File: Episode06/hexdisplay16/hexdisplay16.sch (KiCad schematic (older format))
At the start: 28 parts, among them J1 Conn_01x05, J10 Conn_01x16, J2 Conn_01x05, J3 Conn_01x05, J4 Conn_01x05, J5 Conn_01x05, J6 Conn_01x05, J7 Conn_01x05, J8 Conn_01x05, J9 Conn_01x02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

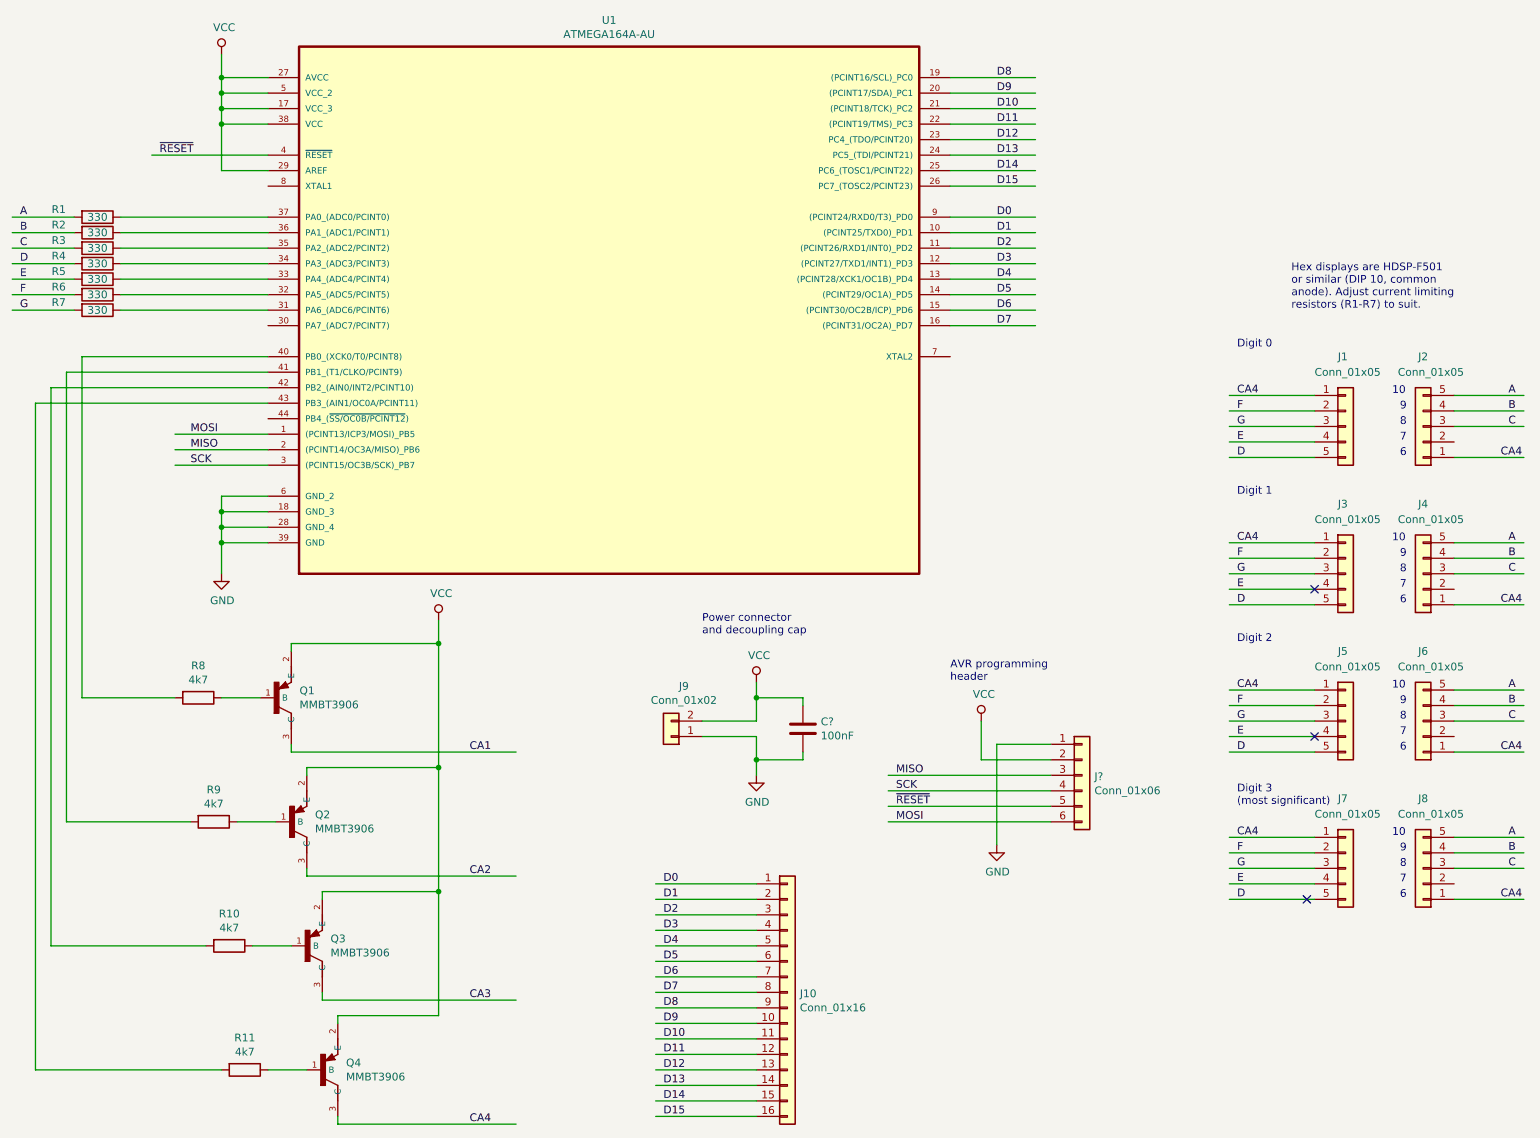
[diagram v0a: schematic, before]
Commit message: use proper DIP-10 connectors for hex displays
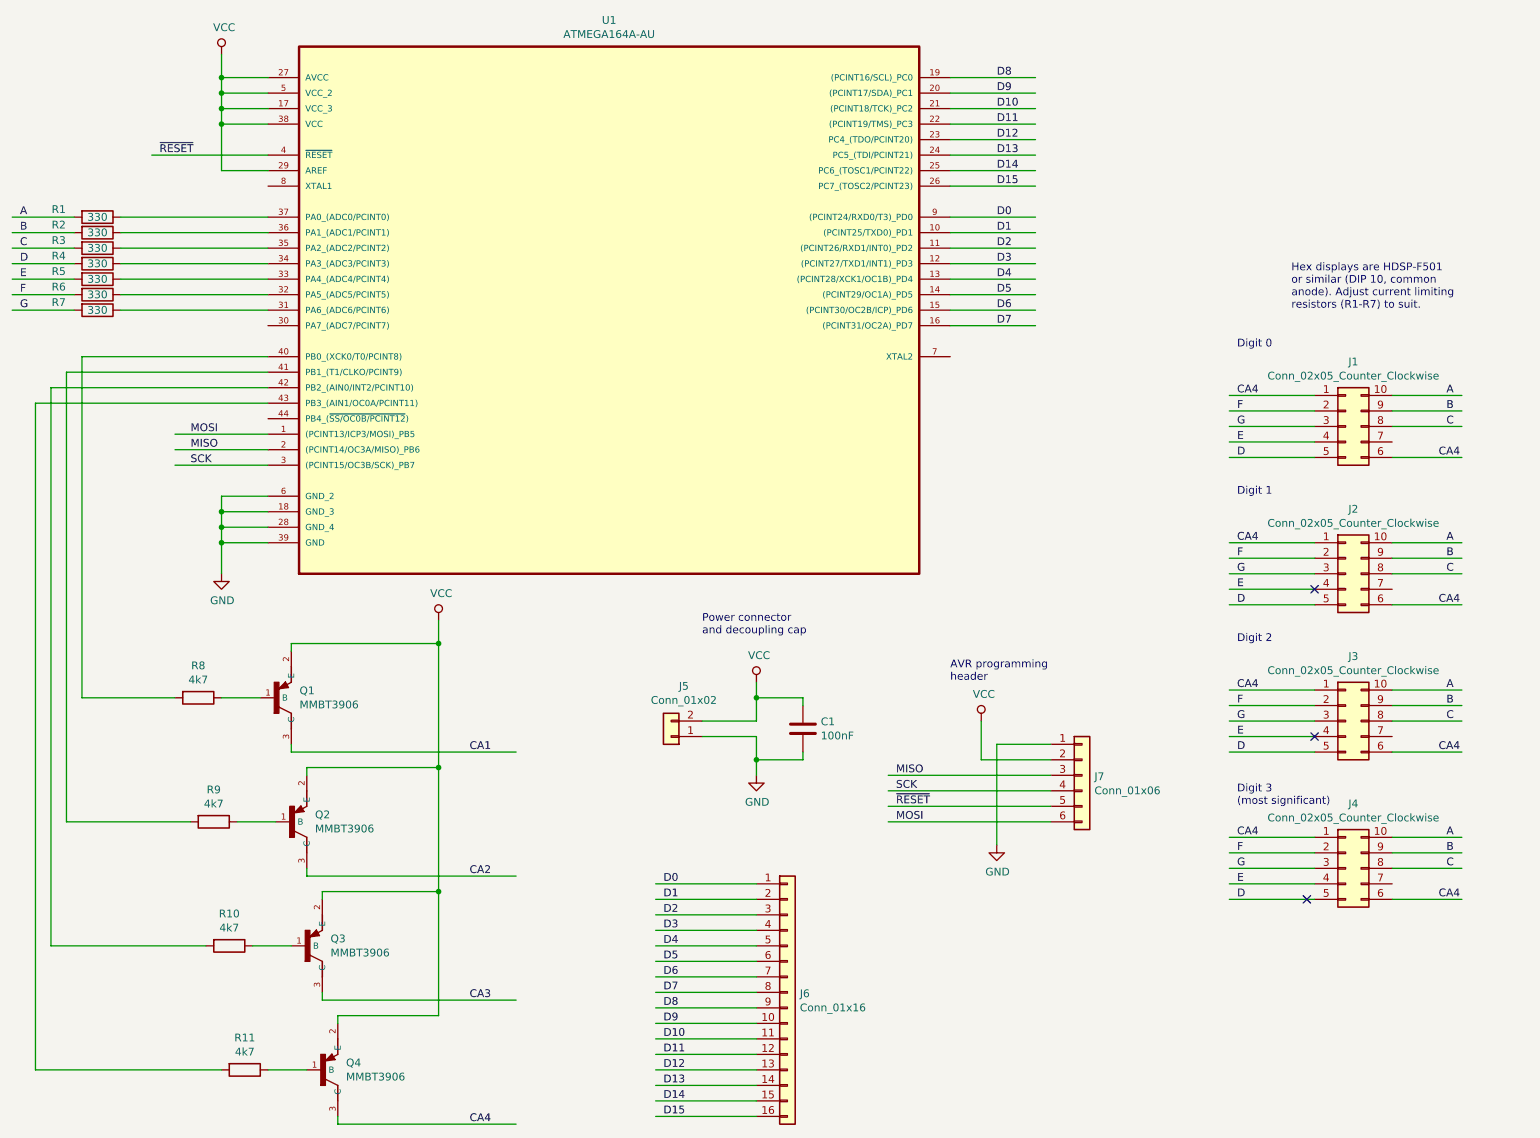
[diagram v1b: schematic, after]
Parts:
- removed J1, J2, J3, J4, J5, J6, J7, J8: Conn_01x05, symbol Connector_Generic:Conn_01x05
- added J1, J2, J3, J4: Conn_02x05_Counter_Clockwise, symbol Connector_Generic:Conn_02x05_Counter_Clockwise
- gave numbers to parts that had none: 2
- renumbered J9 to J5, J10 to J6
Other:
- note removed: "10"
- note removed: "6"
- note removed: "7"
- note removed: "8"
- note removed: "9"
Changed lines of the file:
@@
 CA4
 Wire Wire Line
-	9900 3450 10350 3450
-Text Label 10200 3450 0    50   ~ 0
-CA4
-Wire Wire Line
-	9900 3050 10350 3050
-Text Label 10250 3050 0    50   ~ 0
+	9500 3450 9950 3450
+Text Label 9800 3450 0    50   ~ 0
+CA4
+Wire Wire Line
+	9500 3050 9950 3050
+Text Label 9850 3050 0    50   ~ 0
 A
 Wire Wire Line
-	9900 3150 10350 3150
-Text Label 10250 3150 0    50   ~ 0
+	9500 3150 9950 3150
+Text Label 9850 3150 0    50   ~ 0
 B
 Wire Wire Line
-	9900 3250 10350 3250
-Text Label 10250 3250 0    50   ~ 0
+	9500 3250 9950 3250
+Text Label 9850 3250 0    50   ~ 0
 C
 Wire Wire Line
@@
 $EndComp
 $Comp
-L device:C C?
+L device:C C1
 U 1 1 606D296E
 P 5700 5200
-F 0 "C?" H 5815 5246 50  0000 L CNN
+F 0 "C1" H 5815 5246 50  0000 L CNN
 F 1 "100nF" H 5815 5155 50  0000 L CNN
 F 2 "" H 5738 5050 50  0001 C CNN
@@
 D15
 $Comp
-L Connector_Generic:Conn_01x02 J9
+L Connector_Generic:Conn_01x02 J5
 U 1 1 6044CE3B
 P 4850 5250
-F 0 "J9" H 4768 4925 50  0000 C CNN
+F 0 "J5" H 4768 4925 50  0000 C CNN
 F 1 "Conn_01x02" H 4768 5016 50  0000 C CNN
 F 2 "" H 4850 5250 50  0001 C CNN
@@
 $EndComp
 $Comp
-L Connector_Generic:Conn_01x16 J10
+L Connector_Generic:Conn_01x16 J6
 U 1 1 6044F3A1
 P 5600 6900
-F 0 "J10" H 5680 6892 50  0000 L CNN
+F 0 "J6" H 5680 6892 50  0000 L CNN
 F 1 "Conn_01x16" H 5680 6801 50  0000 L CNN
 F 2 "" H 5600 6900 50  0001 C CNN
@@
 $EndComp
 $Comp
-L Connector_Generic:Conn_01x05 J1
-U 1 1 60451854
-P 9200 3250
-F 0 "J1" H 9150 3700 50  0000 L CNN
-F 1 "Conn_01x05" H 9000 3600 50  0000 L CNN
-F 2 "" H 9200 3250 50  0001 C CNN
-F 3 "~" H 9200 3250 50  0001 C CNN
-	1    9200 3250
-	1    0    0    -1
-$EndComp
-$Comp
-L Connector_Generic:Conn_01x05 J3
-U 1 1 604CA7D9
-P 9200 4200
-F 0 "J3" H 9150 4650 50  0000 L CNN
-F 1 "Conn_01x05" H 9000 4550 50  0000 L CNN
-F 2 "" H 9200 4200 50  0001 C CNN
-F 3 "~" H 9200 4200 50  0001 C CNN
-	1    9200 4200
-	1    0    0    -1
-$EndComp
-$Comp
-L Connector_Generic:Conn_01x05 J5
-U 1 1 604DED1F
-P 9200 5150
-F 0 "J5" H 9150 5600 50  0000 L CNN
-F 1 "Conn_01x05" H 9000 5500 50  0000 L CNN
-F 2 "" H 9200 5150 50  0001 C CNN
-F 3 "~" H 9200 5150 50  0001 C CNN
-	1    9200 5150
-	1    0    0    -1
-$EndComp
-$Comp
-L Connector_Generic:Conn_01x05 J7
-U 1 1 604EEED1
-P 9200 6100
-F 0 "J7" H 9150 6550 50  0000 L CNN
-F 1 "Conn_01x05" H 9000 6450 50  0000 L CNN
-F 2 "" H 9200 6100 50  0001 C CNN
-F 3 "~" H 9200 6100 50  0001 C CNN
-	1    9200 6100
-	1    0    0    -1
-$EndComp
-$Comp
-L Connector_Generic:Conn_01x06 J?
+L Connector_Generic:Conn_01x06 J7
 U 1 1 604FDEE5
 P 7500 5500
-F 0 "J?" H 7580 5492 50  0000 L CNN
+F 0 "J7" H 7580 5492 50  0000 L CNN
 F 1 "Conn_01x06" H 7580 5401 50  0000 L CNN
 F 2 "" H 7500 5500 50  0001 C CNN
@@
 	1    0    0    -1
 $EndComp
-$Comp
-L Connector_Generic:Conn_01x05 J2
-U 1 1 60559034
-P 9700 3250
-F 0 "J2" H 9700 2800 50  0000 C CNN
-F 1 "Conn_01x05" H 9650 2900 50  0000 C CNN
-F 2 "" H 9700 3250 50  0001 C CNN
-F 3 "~" H 9700 3250 50  0001 C CNN
-	1    9700 3250
-	-1   0    0    1
-$EndComp
-Text Notes 9500 3050 0    50   ~ 0
-10
-Text Notes 9550 3150 0    50   ~ 0
-9
-Text Notes 9550 3250 0    50   ~ 0
-8
-Text Notes 9550 3350 0    50   ~ 0
-7
-Text Notes 9550 3450 0    50   ~ 0
-6
-$Comp
-L Connector_Generic:Conn_01x05 J4
-U 1 1 6055B61D
-P 9700 4200
-F 0 "J4" H 9700 3750 50  0000 C CNN
-F 1 "Conn_01x05" H 9650 3850 50  0000 C CNN
-F 2 "" H 9700 4200 50  0001 C CNN
-F 3 "~" H 9700 4200 50  0001 C CNN
-	1    9700 4200
-	-1   0    0    1
-$EndComp
-Text Notes 9500 4000 0    50   ~ 0
-10
-Text Notes 9550 4100 0    50   ~ 0
-9
-Text Notes 9550 4200 0    50   ~ 0
-8
-Text Notes 9550 4300 0    50   ~ 0
-7
-Text Notes 9550 4400 0    50   ~ 0
-6
-$Comp
-L Connector_Generic:Conn_01x05 J6
-U 1 1 60567993
-P 9700 5150
-F 0 "J6" H 9700 4700 50  0000 C CNN
-F 1 "Conn_01x05" H 9650 4800 50  0000 C CNN
-F 2 "" H 9700 5150 50  0001 C CNN
-F 3 "~" H 9700 5150 50  0001 C CNN
-	1    9700 5150
-	-1   0    0    1
-$EndComp
-Text Notes 9500 4950 0    50   ~ 0
-10
-Text Notes 9550 5050 0    50   ~ 0
-9
-Text Notes 9550 5150 0    50   ~ 0
-8
-Text Notes 9550 5250 0    50   ~ 0
-7
-Text Notes 9550 5350 0    50   ~ 0
-6
-$Comp
-L Connector_Generic:Conn_01x05 J8
-U 1 1 60567BE4
-P 9700 6100
-F 0 "J8" H 9700 5650 50  0000 C CNN
-F 1 "Conn_01x05" H 9650 5750 50  0000 C CNN
-F 2 "" H 9700 6100 50  0001 C CNN
-F 3 "~" H 9700 6100 50  0001 C CNN
-	1    9700 6100
-	-1   0    0    1
-$EndComp
-Text Notes 9500 5900 0    50   ~ 0
-10
-Text Notes 9550 6000 0    50   ~ 0
-9
-Text Notes 9550 6100 0    50   ~ 0
-8
-Text Notes 9550 6200 0    50   ~ 0
-7
-Text Notes 9550 6300 0    50   ~ 0
-6
 Text Notes 8500 5700 0    50   ~ 0
 Digit 3\n(most significant)
@@
 E
 Wire Wire Line
-	9900 4400 10350 4400
-Text Label 10200 4400 0    50   ~ 0
-CA4
-Wire Wire Line
-	9900 4000 10350 4000
-Text Label 10250 4000 0    50   ~ 0
+	9500 4400 9950 4400
+Text Label 9800 4400 0    50   ~ 0
+CA4
+Wire Wire Line
+	9500 4000 9950 4000
+Text Label 9850 4000 0    50   ~ 0
 A
 Wire Wire Line
-	9900 4100 10350 4100
-Text Label 10250 4100 0    50   ~ 0
+	9500 4100 9950 4100
+Text Label 9850 4100 0    50   ~ 0
 B
 Wire Wire Line
-	9900 4200 10350 4200
-Text Label 10250 4200 0    50   ~ 0
+	9500 4200 9950 4200
+Text Label 9850 4200 0    50   ~ 0
 C
 Wire Wire Line
-	9900 5350 10350 5350
-Text Label 10200 5350 0    50   ~ 0
-CA4
-Wire Wire Line
-	9900 4950 10350 4950
-Text Label 10250 4950 0    50   ~ 0
+	9500 5350 9950 5350
+Text Label 9800 5350 0    50   ~ 0
+CA4
+Wire Wire Line
+	9500 4950 9950 4950
+Text Label 9850 4950 0    50   ~ 0
 A
 Wire Wire Line
-	9900 5050 10350 5050
-Text Label 10250 5050 0    50   ~ 0
+	9500 5050 9950 5050
+Text Label 9850 5050 0    50   ~ 0
 B
 Wire Wire Line
-	9900 5150 10350 5150
-Text Label 10250 5150 0    50   ~ 0
+	9500 5150 9950 5150
+Text Label 9850 5150 0    50   ~ 0
 C
 Wire Wire Line
-	9900 6300 10350 6300
-Text Label 10200 6300 0    50   ~ 0
-CA4
-Wire Wire Line
-	9900 5900 10350 5900
-Text Label 10250 5900 0    50   ~ 0
+	9500 6300 9950 6300
+Text Label 9800 6300 0    50   ~ 0
+CA4
+Wire Wire Line
+	9500 5900 9950 5900
+Text Label 9850 5900 0    50   ~ 0
 A
 Wire Wire Line
-	9900 6000 10350 6000
-Text Label 10250 6000 0    50   ~ 0
+	9500 6000 9950 6000
+Text Label 9850 6000 0    50   ~ 0
 B
 Wire Wire Line
-	9900 6100 10350 6100
-Text Label 10250 6100 0    50   ~ 0
+	9500 6100 9950 6100
+Text Label 9850 6100 0    50   ~ 0
 C
+$Comp
+L Connector_Generic:Conn_02x05_Counter_Clockwise J1
+U 1 1 6060FA50
+P 9200 3250
+F 0 "J1" H 9250 3667 50  0000 C CNN
+F 1 "Conn_02x05_Counter_Clockwise" H 9250 3576 50  0000 C CNN
+F 2 "" H 9200 3250 50  0001 C CNN
+F 3 "~" H 9200 3250 50  0001 C CNN
+	1    9200 3250
+	1    0    0    -1
+$EndComp
+$Comp
+L Connector_Generic:Conn_02x05_Counter_Clockwise J2
+U 1 1 60639211
+P 9200 4200
+F 0 "J2" H 9250 4617 50  0000 C CNN
+F 1 "Conn_02x05_Counter_Clockwise" H 9250 4526 50  0000 C CNN
+F 2 "" H 9200 4200 50  0001 C CNN
+F 3 "~" H 9200 4200 50  0001 C CNN
+	1    9200 4200
+	1    0    0    -1
+$EndComp
+$Comp
+L Connector_Generic:Conn_02x05_Counter_Clockwise J3
+U 1 1 6064A1C9
+P 9200 5150
+F 0 "J3" H 9250 5567 50  0000 C CNN
+F 1 "Conn_02x05_Counter_Clockwise" H 9250 5476 50  0000 C CNN
+F 2 "" H 9200 5150 50  0001 C CNN
+F 3 "~" H 9200 5150 50  0001 C CNN
+	1    9200 5150
+	1    0    0    -1
+$EndComp
+$Comp
+L Connector_Generic:Conn_02x05_Counter_Clockwise J4
+U 1 1 6064A521
+P 9200 6100
+F 0 "J4" H 9250 6517 50  0000 C CNN
+F 1 "Conn_02x05_Counter_Clockwise" H 9250 6426 50  0000 C CNN
+F 2 "" H 9200 6100 50  0001 C CNN
+F 3 "~" H 9200 6100 50  0001 C CNN
+	1    9200 6100
+	1    0    0    -1
+$EndComp
 $EndSCHEMATC
